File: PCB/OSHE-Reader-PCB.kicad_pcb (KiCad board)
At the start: 4 copper layers, 115 x 100 mm, 79 parts, among them J1 2171750001, J2 112L-TDA0, J3 Conn_01x24_MountingPin, J4 S2B-PH-K-SLFSN, Q1 PNP, Q2 Si1308EDL, SW1 SW_Push, SW2 SW_Push, SW3 SW_Push, SW4 SW_Push, SW5 SW_Push, U1 BQ2057CSNTR, U2 IRF7326D2TRPBF, U3 TPS5432DDA

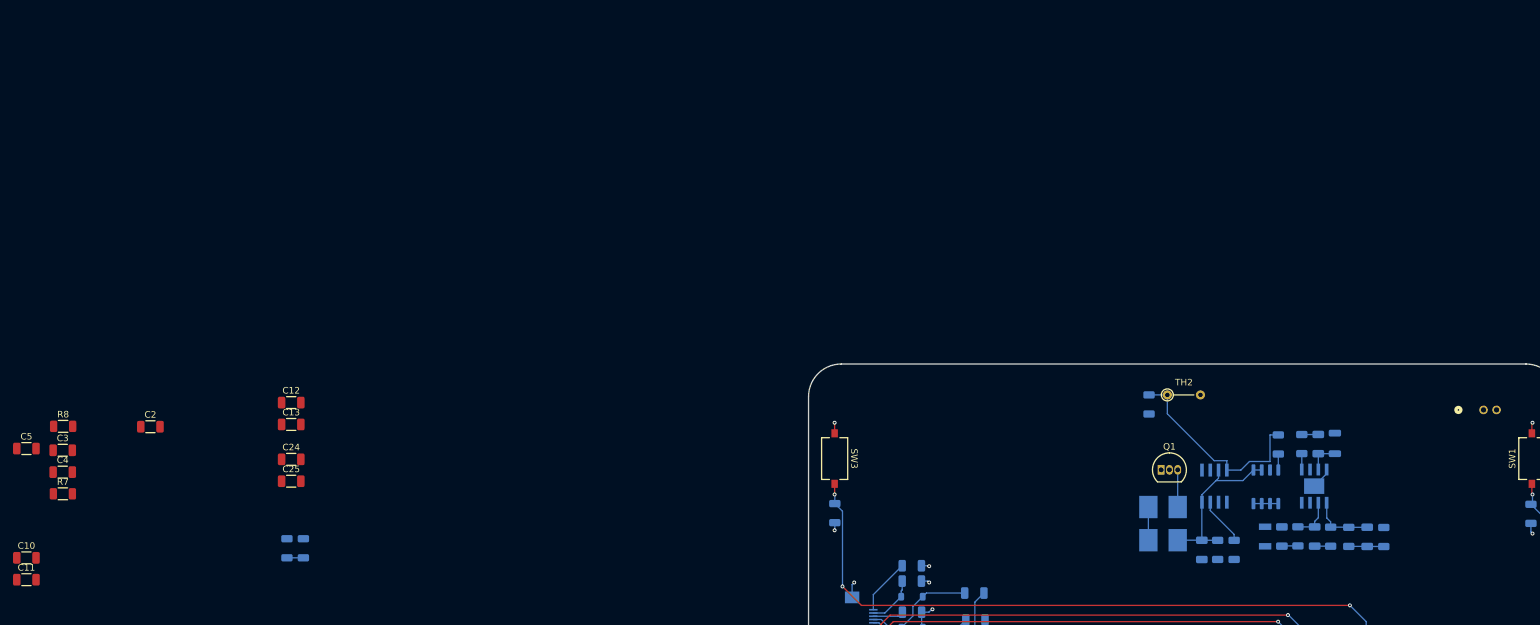
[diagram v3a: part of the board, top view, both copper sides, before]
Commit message: Re-did buck converter schematic sheet to more closely resemble TI's datasheet, implemented buck converter on PCB following TI's datasheet layout example
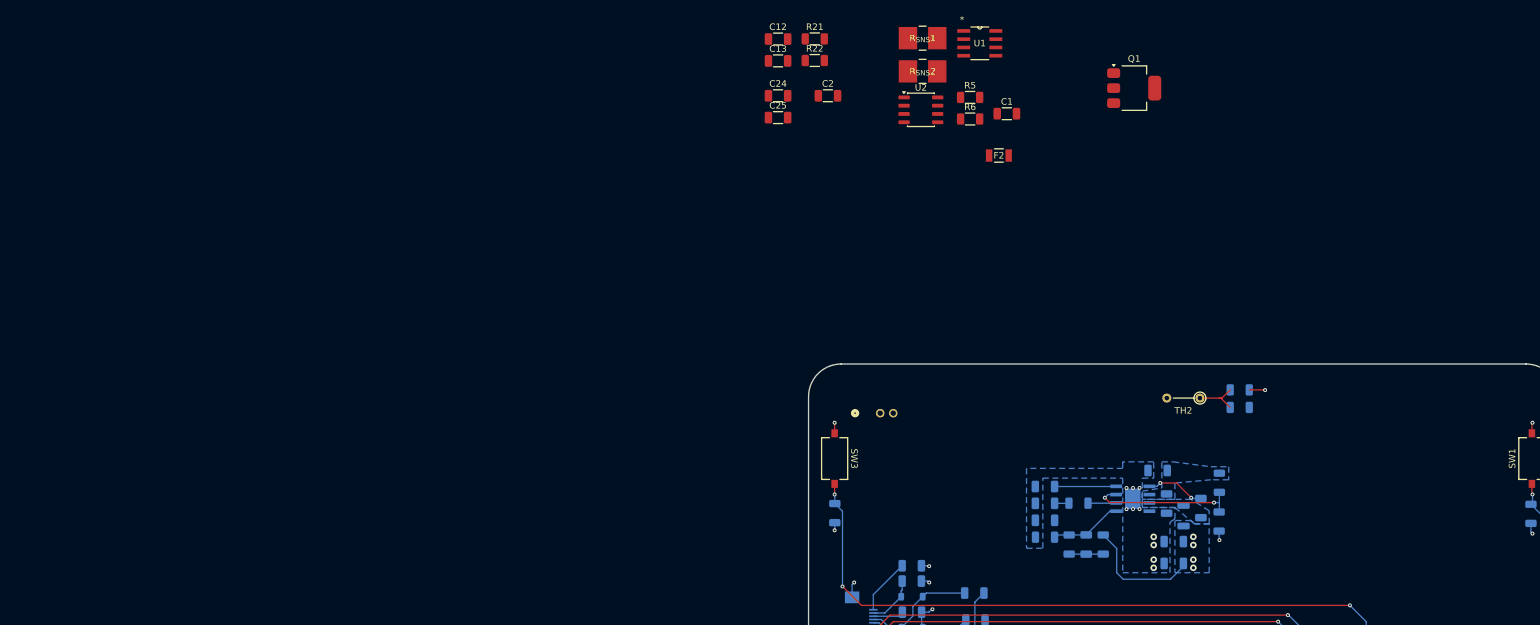
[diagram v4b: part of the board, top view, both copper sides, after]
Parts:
- removed R10: 0, Resistor_SMD:R_1206_3216Metric
- C1, F2, R21, R22, R5, R6, R_{SNS}1, R_{SNS}2, U1, U2: moved to F.Cu
- C10, C11, C3, C4, C5: moved to B.Cu
- Q1: value PNP -> Q_PNP_BCEC; footprint Package_TO_SOT_THT:TO-92_Inline -> Package_TO_SOT_SMD:SOT-223
- R7: value 66.5 -> 66.5k; moved to B.Cu
- R8: value 45.3 -> 45.3k; moved to B.Cu
- U3: value TPS5432DDA -> TPS5432DDAR
- moved R8 177.8 mm to (95.5, 104.7), turned to -90 degrees
- moved R7 177.3 mm to (95.5, 98.7), turned to -90 degrees
- moved C11 176.0 mm to (88.5, 107.7)
- moved C10 175.9 mm to (88.5, 111.1)
- moved C3 169.4 mm to (87.4, 101.9), turned to -90 degrees
- moved C4 167.9 mm to (86.0, 96.8), turned to 180 degrees
- moved C5 156.3 mm to (68.7, 99.3), turned to 180 degrees
- moved C2 115.6 mm to (35.5, 39.4)
- moved R21 112.5 mm to (33.5, 30.7), turned to 0 degrees
- moved R22 108.4 mm to (33.5, 34.0), turned to 0 degrees
- moved C12 93.2 mm to (27.8, 30.7)
- moved C13 93.2 mm to (27.8, 34.0)
- moved C24 93.2 mm to (27.8, 39.4)
- moved C25 93.2 mm to (27.8, 42.7)
- moved J4 92.5 mm to (43.5, 88.0)
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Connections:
- net /Buck Converter/5 renamed Net-(U3-VSENSE)
- net /Buck Converter/6 renamed Net-(U3-COMP)
- C3 pad 1: GND -> /Buck Converter/VIN
- C3 pad 2: /Buck Converter/VIN -> GND
- C4 pad 1: GND -> /Buck Converter/VIN
- C4 pad 2: /Buck Converter/VIN -> GND
- C5 pad 1: GND -> Net-(U3-SS)
- C5 pad 2: Net-(U3-SS) -> GND
- C8 pad 1: /Buck Converter/3 -> Net-(U3-BOOT)
- C8 pad 2: Net-(C8-Pad2) -> Net-(U3-PH)
- L1 pad 1: /Buck Converter/3 -> Net-(U3-PH)
- Q1 pad 1: /Battery Charging/BAT+ -> Net-(Q1-B)
- Q1 pad 2: Net-(Q1-B) -> /Battery Charging/BAT+
- U3 pad 1: /Buck Converter/1 -> Net-(U3-BOOT)
- U3 pad 3: /Buck Converter/3 -> Net-(U3-PH)
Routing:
- net /Battery Charging/VBUS: track 28.1 -> 0.00 mm
- net /Battery Charging/TS: track 31.8 -> 7.40 mm
- net Net-(U3-EN): track 0.00 -> 22.9 mm, vias 0 -> 2
- net +3V3: track 24.0 -> 42.6 mm, vias 11 -> 15
- net Net-(U3-SS): track 0.00 -> 9.46 mm
- net Net-(U3-BOOT): track 0.00 -> 9.08 mm, vias 0 -> 2
- net Net-(U1-CC): track 7.36 -> 0.00 mm
- net Net-(Q1-E): track 5.70 -> 0.00 mm
- net Net-(R_{SNS}1-Pad2): track 5.09 -> 0.00 mm
- net /Buck Converter/3: track 4.98 -> 0.00 mm
- net /Battery Charging/VOUT: track 3.81 -> 0.00 mm
- net Net-(C8-Pad2): track 2.53 -> 0.00 mm
- net Net-(U4-GPIO0): track 2.52 -> 0.00 mm
- net /Buck Converter/1: track 2.44 -> 0.00 mm
- net Net-(U3-COMP): track 6.51 -> 4.35 mm
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- added copper zone on B.Cu, net +3V3
- added copper zone on B.Cu, net /Buck Converter/VIN
- added copper zone on B.Cu, net GND
- added copper zone on B.Cu, net Net-(U3-PH)

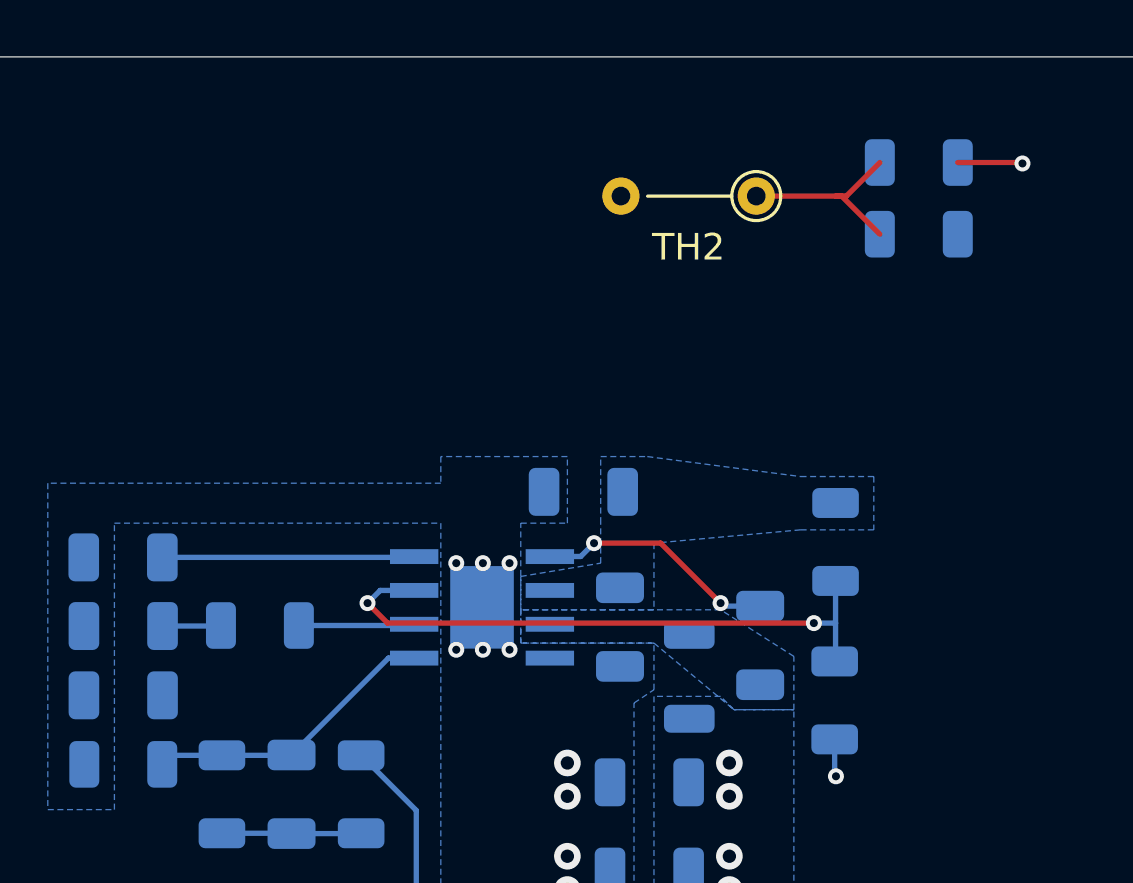
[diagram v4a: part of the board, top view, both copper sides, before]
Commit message: PCB Update
updated some PCB traces
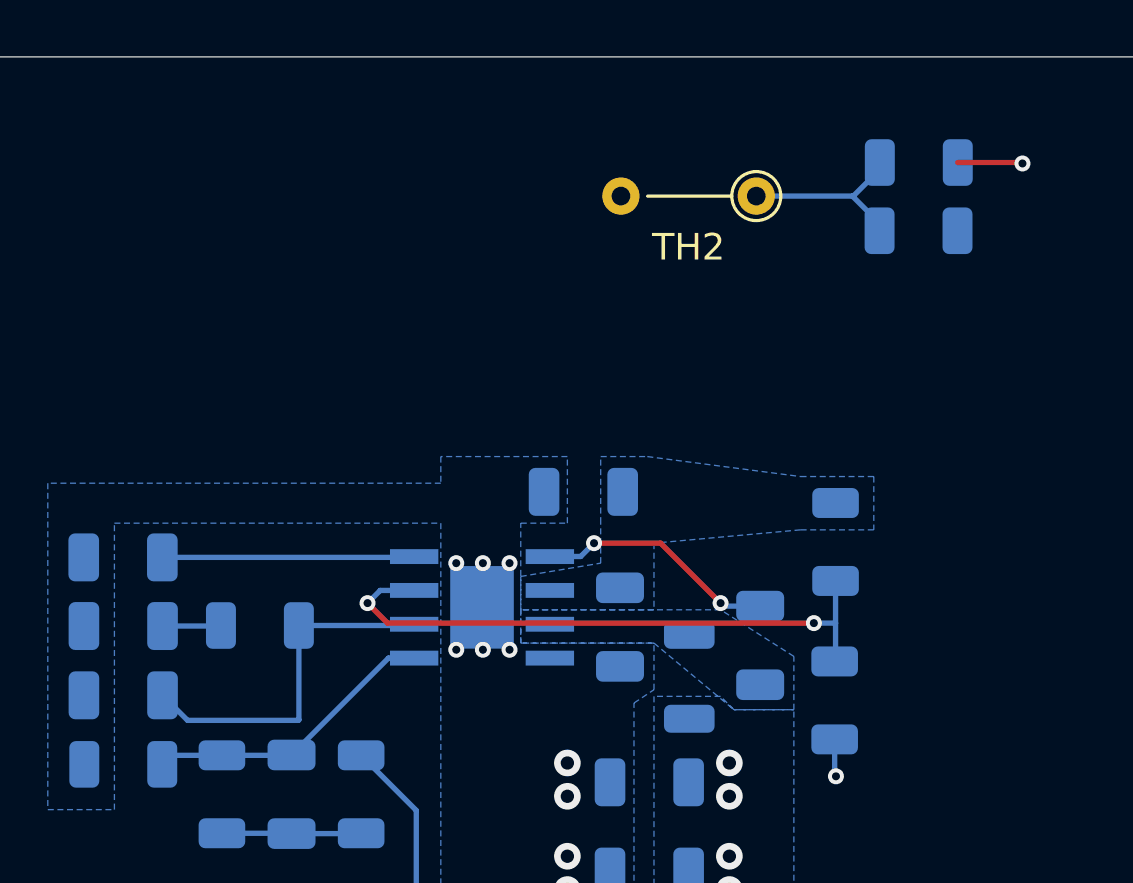
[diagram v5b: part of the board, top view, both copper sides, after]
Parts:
- moved R3 0.13 mm to (98.6, 87.0)
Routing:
- net Net-(U3-COMP): track 4.35 -> 13.4 mm
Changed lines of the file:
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@@
 	(footprint "Resistor_SMD:R_1206_3216Metric"
 		(layer "B.Cu")
-		(at 98.61 87.155 180)
+		(at 98.6 87.025 180)
 		(descr "Resistor SMD 1206 (3216 Metric), square (rectangular) end terminal, IPC-7351 nominal, (Body size source: IPC-SM-782 page 72, https://www.pcb-3d.com/wordpress/wp-content/uploads/ipc-sm-782a_amendment_1_and_2.pdf), generated with kicad-footprint-generator")
 		(tags "resistor")
@@
 	)
 	(segment
-		(start 95.8883 85.7242)
+		(start 92.5108 85.725)
+		(end 92.51 85.7242)
+		(width 0.2)
+		(layer "B.Cu")
+		(net 52)
+	)
+	(segment
+		(start 97.1375 87.025)
+		(end 97.1375 86.74375)
+		(width 0.2)
+		(layer "B.Cu")
+		(net 52)
+	)
+	(segment
+		(start 97.1475 84.7275)
 		(end 97.1475 84.465)
 		(width 0.2)
-		(layer "F.Cu")
+		(layer "B.Cu")
 		(net 52)
 	)
 	(segment
-		(start 95.5 85.7242)
-		(end 95.8883 85.7242)
+		(start 97.1375 87.025)
+		(end 97.1375 86.8425)
 		(width 0.2)
-		(layer "F.Cu")
+		(layer "B.Cu")
 		(net 52)
 	)
 	(segment
-		(start 95.5 85.7242)
-		(end 92.51 85.7242)
+		(start 96.1508 85.7242)
+		(end 97.1475 84.7275)
 		(width 0.2)
-		(layer "F.Cu")
+		(layer "B.Cu")
 		(net 52)
 	)
 	(segment
-		(start 95.7167 85.7242)
-		(end 95.5 85.7242)
+		(start 97.1375 86.74375)
+		(end 96.11795 85.7242)
 		(width 0.2)
-		(layer "F.Cu")
+		(layer "B.Cu")
 		(net 52)
 	)
 	(segment
-		(start 97.1475 87.155)
-		(end 95.7167 85.7242)
+		(start 96.11795 85.7242)
+		(end 92.51 85.7242)
 		(width 0.2)
-		(layer "F.Cu")
+		(layer "B.Cu")
 		(net 52)
 	)
@@
 		(width 0.2)
 		(layer "B.Cu")
+		(net 75)
+	)
+	(segment
+		(start 75.344173 105.380827)
+		(end 75.344173 101.840401)
+		(width 0.2)
+		(layer "B.Cu")
+		(net 75)
+	)
+	(segment
+		(start 75.325 105.4)
+		(end 75.344173 105.380827)
+		(width 0.2)
+		(layer "B.Cu")
+		(net 75)
+	)
+	(segment
+		(start 71.166272 105.4)
+		(end 75.325 105.4)
+		(width 0.2)
+		(layer "B.Cu")
+		(net 75)
+	)
+	(segment
+		(start 70.226673 104.460401)
+		(end 71.166272 105.4)
+		(width 0.2)
+		(layer "B.Cu")

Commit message: PCB Update
Updated the PCB
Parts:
- C1, C2, F2, Q1, R5, R6, R_{SNS}1, R_{SNS}2, U1, U2: moved to B.Cu
- moved R_{SNS}1 75.4 mm to (61.1, 105.1), turned to -90 degrees
- moved R_{SNS}2 69.5 mm to (48.9, 105.1), turned to 90 degrees
- moved U1 64.3 mm to (51.0, 95.1)
- moved C1 61.0 mm to (53.8, 102.5), turned to -90 degrees
- moved R6 59.5 mm to (56.5, 102.5), turned to -90 degrees
- moved U2 56.4 mm to (60.0, 97.0)
- moved C2 55.5 mm to (41.8, 94.5), turned to -90 degrees
- moved Q1 54.5 mm to (60.6, 88.2)
- moved F2 50.5 mm to (86.1, 92.7)
- moved R5 48.0 mm to (53.5, 87.5), turned to -90 degrees
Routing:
- net /Battery Charging/VBUS: track 0.00 -> 136.6 mm, vias 0 -> 2
- net /Battery Charging/TS: track 7.19 -> 59.5 mm
- net /Battery Charging/BAT+: track 0.00 -> 40.7 mm
- net Net-(Q1-E): track 0.00 -> 36.1 mm, vias 0 -> 2
- net /Battery Charging/VOUT: track 0.00 -> 27.0 mm
- net Net-(R_{SNS}1-Pad2): track 0.00 -> 12.2 mm
- net Net-(U1-CC): track 0.00 -> 8.46 mm
- net Net-(Q1-B): track 0.00 -> 6.41 mm
- net /Buck Converter/VIN: track 0.00 -> 4.16 mm
- net GND: track 64.8 -> 68.4 mm, vias 47 -> 48

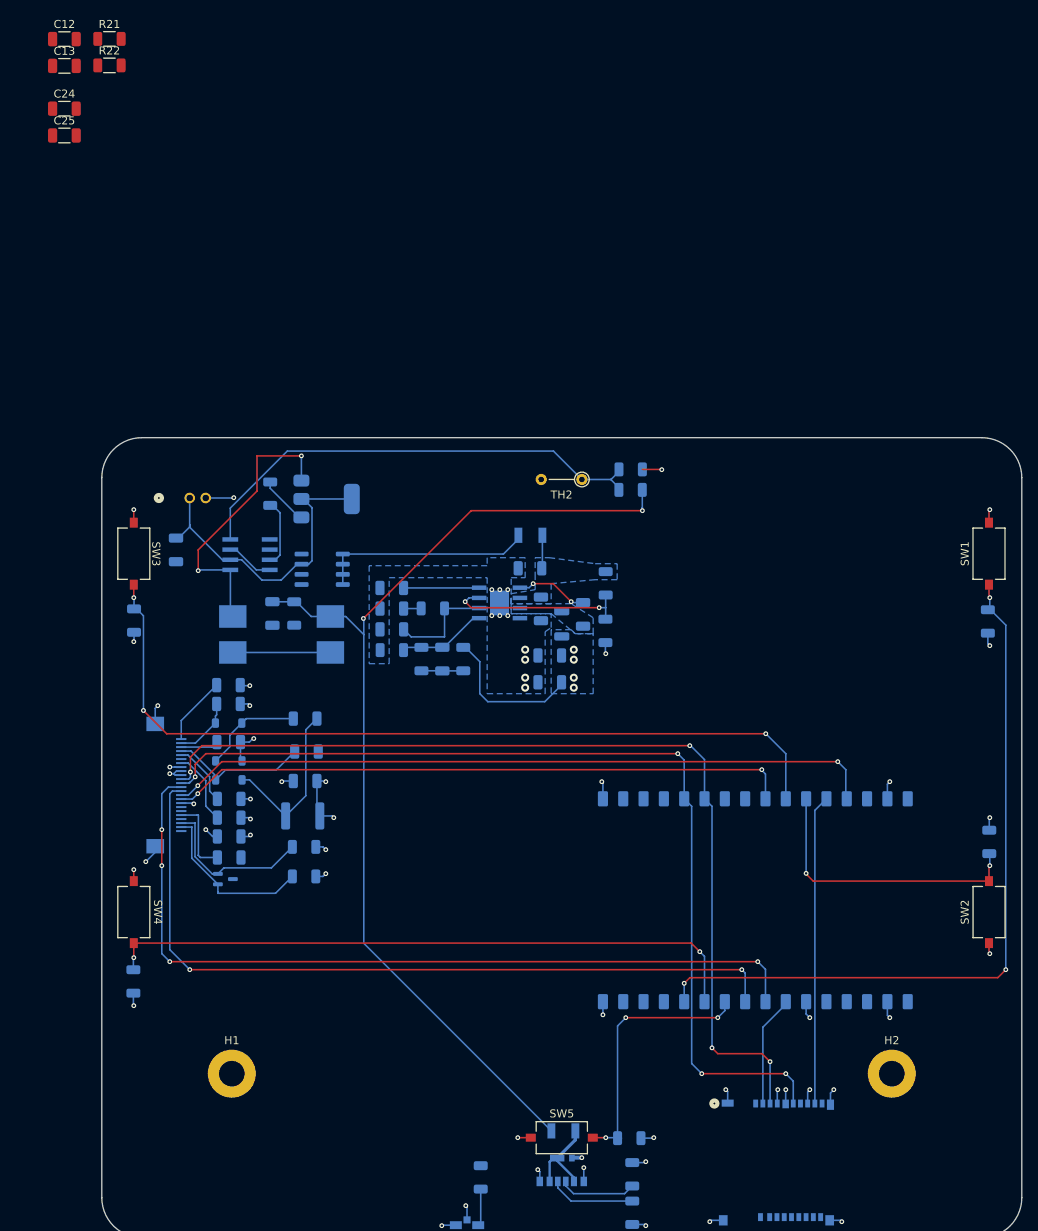
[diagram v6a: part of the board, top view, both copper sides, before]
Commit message: Finished main draft of PCB, TODO: OSHE logo, Peer review
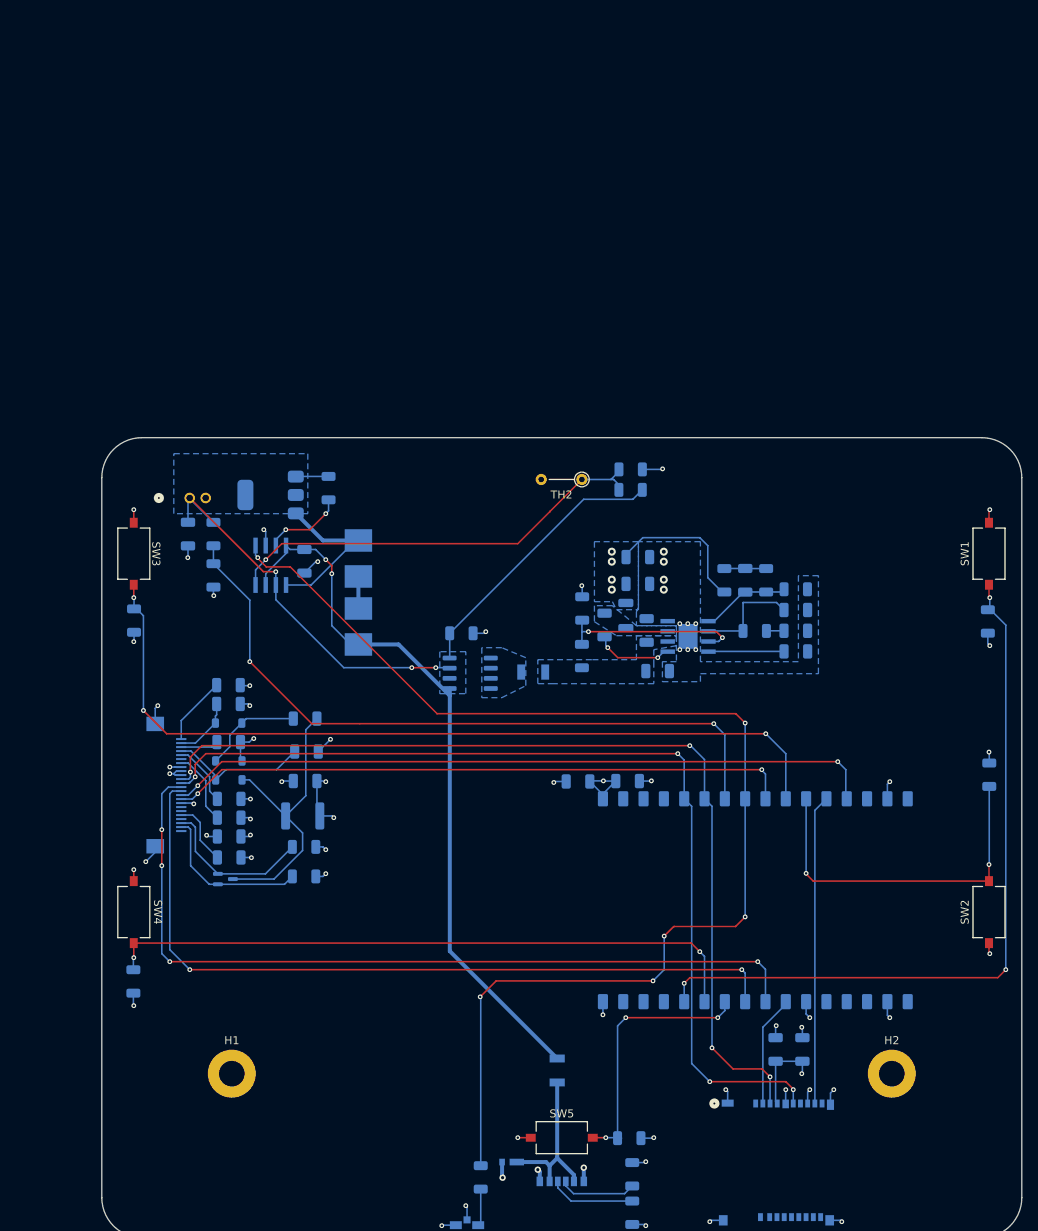
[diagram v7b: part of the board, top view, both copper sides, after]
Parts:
- C12, C13, C24, C25, R21, R22: moved to B.Cu
- moved C24 149.5 mm to (120.1, 157.0), turned to 90 degrees
- moved C25 144.8 mm to (116.7, 157.0), turned to 90 degrees
- moved C13 113.8 mm to (98.2, 123.4)
- moved C12 112.8 mm to (92.0, 123.5), turned to 180 degrees
- moved R22 65.1 mm to (46.5, 97.7), turned to -90 degrees
- moved R21 63.2 mm to (46.5, 92.5), turned to -90 degrees
- moved C5 51.1 mm to (119.3, 107.2), turned to 0 degrees
- moved R13 51.1 mm to (119.2, 99.4), turned to 0 degrees
- moved C6 50.6 mm to (119.2, 104.6), turned to 0 degrees
- moved C7 50.6 mm to (119.2, 102.0), turned to 0 degrees
- moved R12 44.2 mm to (115.5, 98.3), turned to -90 degrees
- moved R9 40.3 mm to (114.1, 104.7), turned to 0 degrees
- moved C9 39.1 mm to (112.9, 98.3), turned to 90 degrees
- moved R11 34.1 mm to (110.3, 98.3), turned to 90 degrees
- moved U3 23.9 mm to (105.8, 105.3), turned to 0 degrees
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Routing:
- net /BAT_STAT: track 0.00 -> 156.3 mm, vias 0 -> 6
- net Net-(U4-GPIO0): track 0.00 -> 87.5 mm, vias 0 -> 2
- net /Battery Charging/VOUT: track 27.0 -> 0.00 mm
- net Net-(Q1-E): track 36.1 -> 20.6 mm, vias 2 -> 0
- net Net-(D2-A): track 21.1 -> 36.5 mm
- net GND: track 68.4 -> 83.5 mm, vias 48 -> 58
- net +3V3: track 42.7 -> 57.7 mm
- net /Battery Charging/VBUS: track 136.6 -> 125.0 mm
- net /Battery Charging/BAT+: track 40.7 -> 50.8 mm, vias 0 -> 3
- net /USB-C-Connector/VBUS: track 11.7 -> 20.8 mm
- net /Buttons/RightButton: track 36.1 -> 44.5 mm
- net Net-(R_{SNS}1-Pad2): track 12.2 -> 4.00 mm
- net /Battery Charging/TS: track 59.5 -> 54.6 mm, vias 0 -> 1
- net /Buck Converter/VIN: track 4.16 -> 0.00 mm
- net Net-(Q1-B): track 6.41 -> 4.10 mm
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- added copper zone on B.Cu, net /Battery Charging/BAT+
- added copper zone on B.Cu, net /Battery Charging/VBUS
- added copper zone on B.Cu, net /Battery Charging/VOUT
